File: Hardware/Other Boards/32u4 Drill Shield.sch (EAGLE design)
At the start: 16 parts, among them U2 XBEE-1B3

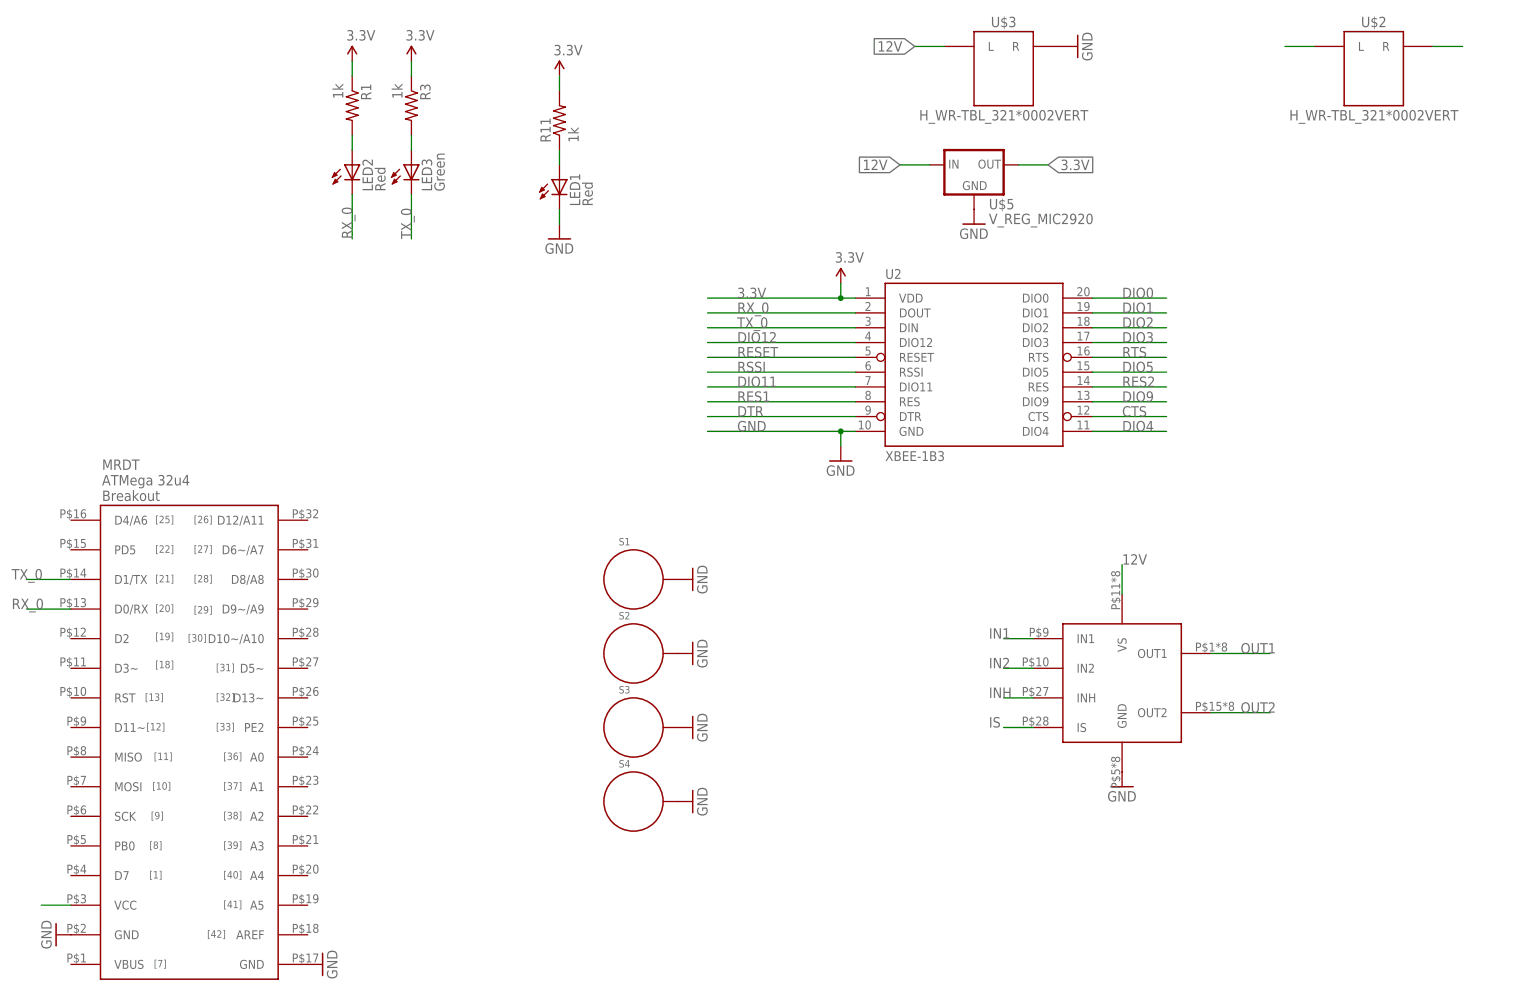
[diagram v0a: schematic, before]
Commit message: Finished shields for aux
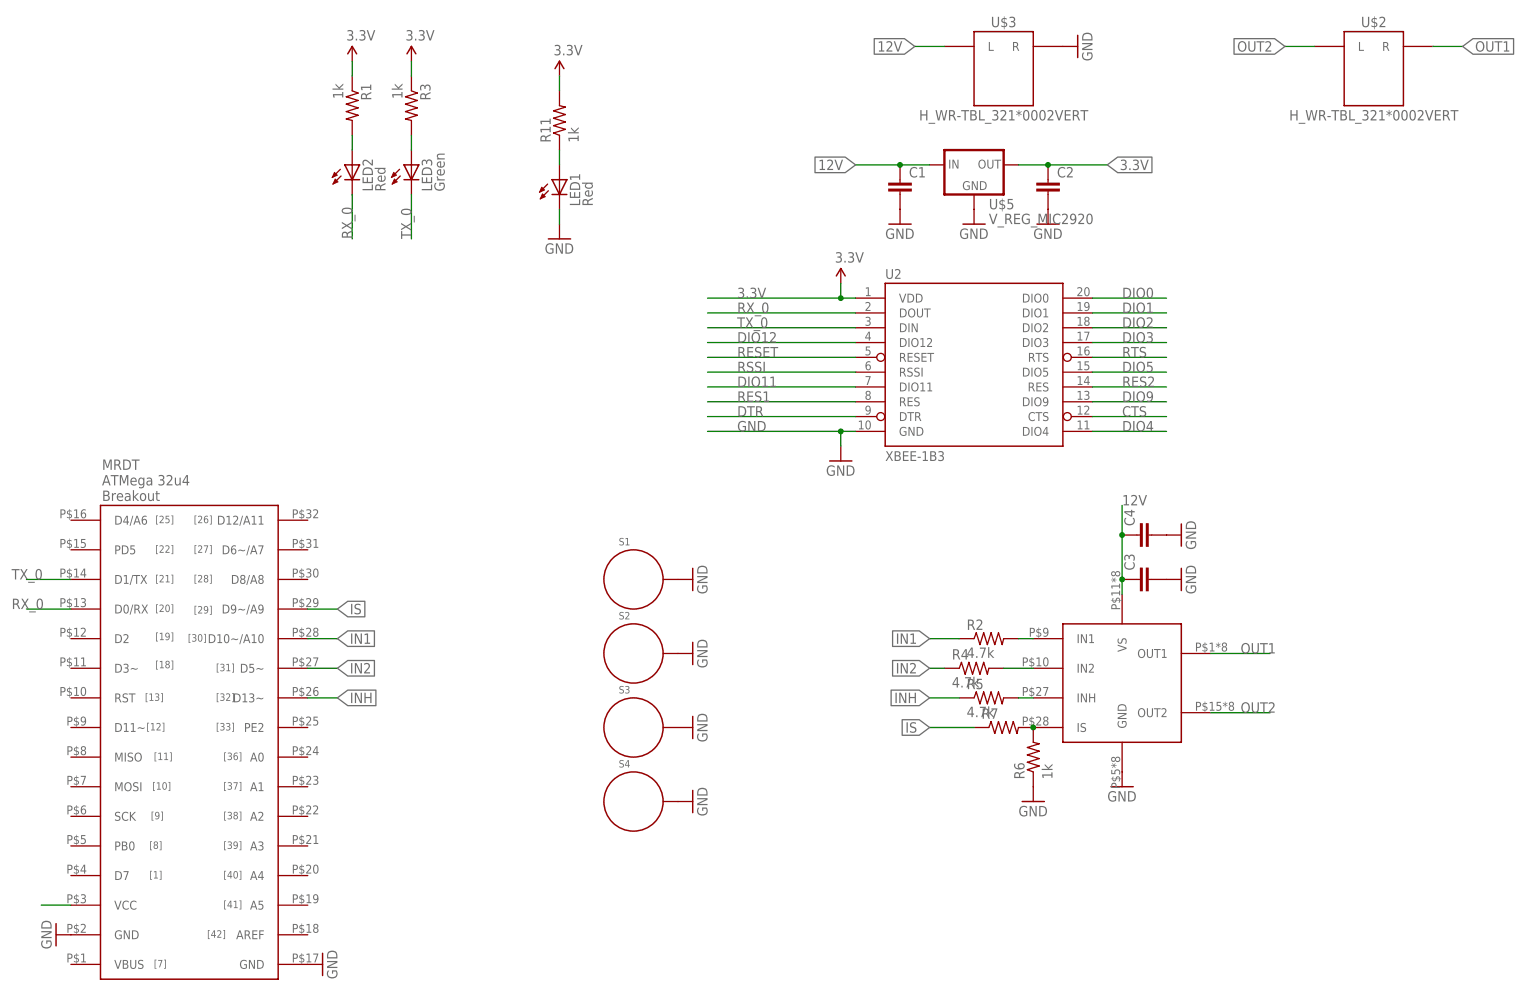
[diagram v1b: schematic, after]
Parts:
- added C1, C2, C3, C4: (no value), SparkFun-Passives:CAP1206
- added R2, R4, R5: 4.7k, SparkFun-Passives:RESISTOR1206
- added R6: 1k, SparkFun-Passives:RESISTOR1206
- added R7: (no value), SparkFun-Passives:RESISTOR1206
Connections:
- new net N$2: R2.2, U$4.IN1
- new net N$3: R4.2, U$4.IN2
- new net N$5: R5.2, U$4.INH
- new net N$6: R6.2, R7.2, U$4.IS
- net 12V: now also C1.1, C3.1, C4.1
- net 3.3V: now also C2.1
- net GND: now also C1.2, C2.2, C3.2, C4.2, R6.1
- net IN1: now also R2.1, U$1.D10~/A10; no longer U$4.IN1
- net IN2: now also R4.1, U$1.D5~; no longer U$4.IN2
- net INH: now also R5.1, U$1.D13~; no longer U$4.INH
- net IS: now also R7.1, U$1.D9~/A9; no longer U$4.IS
- net OUT1: now also U$2.R
- net OUT2: no longer U$2.R
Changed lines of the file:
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@@
 <part name="U$4" library="MRDT-2015-General" deviceset="BTM7752G" device=""/>
 <part name="GND10" library="SparkFun" deviceset="GND" device=""/>
+<part name="C1" library="SparkFun-Passives" deviceset="CAP" device="1206"/>
+<part name="C2" library="SparkFun-Passives" deviceset="CAP" device="1206"/>
+<part name="GND11" library="SparkFun" deviceset="GND" device=""/>
+<part name="GND12" library="SparkFun" deviceset="GND" device=""/>
+<part name="R2" library="SparkFun-Passives" deviceset="RESISTOR" device="1206" value="4.7k"/>
+<part name="R4" library="SparkFun-Passives" deviceset="RESISTOR" device="1206" value="4.7k"/>
+<part name="R5" library="SparkFun-Passives" deviceset="RESISTOR" device="1206" value="4.7k"/>
+<part name="R6" library="SparkFun-Passives" deviceset="RESISTOR" device="1206" value="1k"/>
+<part name="GND13" library="SparkFun" deviceset="GND" device=""/>
+<part name="R7" library="SparkFun-Passives" deviceset="RESISTOR" device="1206"/>
+<part name="C3" library="SparkFun-Passives" deviceset="CAP" device="1206"/>
+<part name="C4" library="SparkFun-Passives" deviceset="CAP" device="1206"/>
+<part name="GND14" library="SparkFun" deviceset="GND" device=""/>
+<part name="GND15" library="SparkFun" deviceset="GND" device=""/>
 </parts>
 <sheets>
@@
 <instance part="U$4" gate="G$1" x="185.42" y="53.34"/>
 <instance part="GND10" gate="1" x="185.42" y="35.56"/>
+<instance part="C1" gate="G$1" x="147.32" y="137.16"/>
+<instance part="C2" gate="G$1" x="172.72" y="137.16"/>
+<instance part="GND11" gate="1" x="147.32" y="132.08"/>
+<instance part="GND12" gate="1" x="172.72" y="132.08"/>
+<instance part="R2" gate="G$1" x="162.56" y="60.96"/>
+<instance part="R4" gate="G$1" x="160.02" y="55.88"/>
+<instance part="R5" gate="G$1" x="162.56" y="50.8"/>
+<instance part="R6" gate="G$1" x="170.18" y="40.64" rot="R90"/>
+<instance part="GND13" gate="1" x="170.18" y="33.02"/>
+<instance part="R7" gate="G$1" x="165.1" y="45.72"/>
+<instance part="C3" gate="G$1" x="190.5" y="71.12" rot="R90"/>
+<instance part="C4" gate="G$1" x="190.5" y="78.74" rot="R90"/>
+<instance part="GND14" gate="1" x="195.58" y="78.74" rot="R90"/>
+<instance part="GND15" gate="1" x="195.58" y="71.12" rot="R90"/>
 </instances>
 <busses>
@@
 <pinref part="GND10" gate="1" pin="GND"/>
 </segment>
+<segment>
+<pinref part="C1" gate="G$1" pin="2"/>
+<pinref part="GND11" gate="1" pin="GND"/>
+</segment>
+<segment>
+<pinref part="C2" gate="G$1" pin="2"/>
+<pinref part="GND12" gate="1" pin="GND"/>
+</segment>
+<segment>
+<pinref part="R6" gate="G$1" pin="1"/>
+<pinref part="GND13" gate="1" pin="GND"/>
+</segment>
+<segment>
+<pinref part="C4" gate="G$1" pin="2"/>
+<pinref part="GND14" gate="1" pin="GND"/>
+</segment>
+<segment>
+<pinref part="C3" gate="G$1" pin="2"/>
+<pinref part="GND15" gate="1" pin="GND"/>
+</segment>
 </net>
 <net name="RESET" class="0">
@@
 <pinref part="U$5" gate="G$1" pin="OUT"/>
 <wire x1="167.64" y1="142.24" x2="172.72" y2="142.24" width="0.1524" layer="91"/>
-<label x="172.72" y="142.24" size="1.778" layer="95" xref="yes"/>
+<label x="182.88" y="142.24" size="1.778" layer="95" xref="yes"/>
+<pinref part="C2" gate="G$1" pin="1"/>
+<wire x1="172.72" y1="142.24" x2="182.88" y2="142.24" width="0.1524" layer="91"/>
+<junction x="172.72" y="142.24"/>
 </segment>
 </net>
@@
 <pinref part="U$5" gate="G$1" pin="IN"/>
 <wire x1="152.4" y1="142.24" x2="147.32" y2="142.24" width="0.1524" layer="91"/>
-<label x="147.32" y="142.24" size="1.778" layer="95" rot="R180" xref="yes"/>
+<label x="139.7" y="142.24" size="1.778" layer="95" rot="R180" xref="yes"/>
+<pinref part="C1" gate="G$1" pin="1"/>
+<wire x1="147.32" y1="142.24" x2="139.7" y2="142.24" width="0.1524" layer="91"/>
+<junction x="147.32" y="142.24"/>
 </segment>
 <segment>
@@
 <segment>
 <pinref part="U$4" gate="G$1" pin="VS"/>
-<wire x1="185.42" y1="68.58" x2="185.42" y2="73.66" width="0.1524" layer="91"/>
-<label x="185.42" y="73.66" size="1.778" layer="95"/>
+<wire x1="185.42" y1="68.58" x2="185.42" y2="71.12" width="0.1524" layer="91"/>
+<label x="185.42" y="83.82" size="1.778" layer="95"/>
+<pinref part="C3" gate="G$1" pin="1"/>
+<wire x1="185.42" y1="71.12" x2="185.42" y2="78.74" width="0.1524" layer="91"/>
+<junction x="185.42" y="71.12"/>
+<pinref part="C4" gate="G$1" pin="1"/>
+<wire x1="185.42" y1="78.74" x2="185.42" y2="83.82" width="0.1524" layer="91"/>
+<junction x="185.42" y="78.74"/>
 </segment>
 </net>
@@
 <label x="205.74" y="58.42" size="1.778" layer="95"/>
 </segment>
+<segment>
+<pinref part="U$2" gate="G$1" pin="R"/>
+<wire x1="238.76" y1="162.56" x2="243.84" y2="162.56" width="0.1524" layer="91"/>
+<label x="243.84" y="162.56" size="1.778" layer="95" xref="yes"/>
+</segment>
 </net>
 <net name="OUT2" class="0">
@@
 </segment>
 <segment>
-<pinref part="U$2" gate="G$1" pin="R"/>
-<wire x1="238.76" y1="162.56" x2="243.84" y2="162.56" width="0.1524" layer="91"/>
-</segment>
-<segment>
 <pinref part="U$2" gate="G$1" pin="L"/>
 <wire x1="218.44" y1="162.56" x2="213.36" y2="162.56" width="0.1524" layer="91"/>
+<label x="213.36" y="162.56" size="1.778" layer="95" rot="R180" xref="yes"/>
+</segment>
+</net>
+<net name="N$2" class="0">
+<segment>
+<pinref part="U$4" gate="G$1" pin="IN1"/>
+<pinref part="R2" gate="G$1" pin="2"/>
+<wire x1="167.64" y1="60.96" x2="170.18" y2="60.96" width="0.1524" layer="91"/>
+</segment>
+</net>
+<net name="N$3" class="0">
+<segment>
+<pinref part="U$4" gate="G$1" pin="IN2"/>
+<pinref part="R4" gate="G$1" pin="2"/>
+<wire x1="165.1" y1="55.88" x2="170.18" y2="55.88" width="0.1524" layer="91"/>
+</segment>
+</net>
+<net name="N$5" class="0">
+<segment>
+<pinref part="U$4" gate="G$1" pin="INH"/>
+<pinref part="R5" gate="G$1" pin="2"/>
+<wire x1="167.64" y1="50.8" x2="170.18" y2="50.8" width="0.1524" layer="91"/>
 </segment>
 </net>
 <net name="IN1" class="0">
 <segment>
-<pinref part="U$4" gate="G$1" pin="IN1"/>
-<wire x1="170.18" y1="60.96" x2="165.1" y2="60.96" width="0.1524" layer="91"/>
-<label x="162.56" y="60.96" size="1.778" layer="95"/>
+<pinref part="R2" gate="G$1" pin="1"/>
+<wire x1="157.48" y1="60.96" x2="152.4" y2="60.96" width="0.1524" layer="91"/>
+<label x="152.4" y="60.96" size="1.778" layer="95" rot="R180" xref="yes"/>
+</segment>
+<segment>
+<pinref part="U$1" gate="G$1" pin="D10~/A10"/>
+<wire x1="45.72" y1="60.96" x2="50.8" y2="60.96" width="0.1524" layer="91"/>
+<label x="50.8" y="60.96" size="1.778" layer="95" xref="yes"/>
 </segment>
 </net>
 <net name="IN2" class="0">
 <segment>
-<pinref part="U$4" gate="G$1" pin="IN2"/>
-<wire x1="170.18" y1="55.88" x2="165.1" y2="55.88" width="0.1524" layer="91"/>
-<label x="162.56" y="55.88" size="1.778" layer="95"/>
+<pinref part="R4" gate="G$1" pin="1"/>
+<wire x1="154.94" y1="55.88" x2="152.4" y2="55.88" width="0.1524" layer="91"/>
+<label x="152.4" y="55.88" size="1.778" layer="95" rot="R180" xref="yes"/>
+</segment>
+<segment>
+<pinref part="U$1" gate="G$1" pin="D5~"/>
+<wire x1="45.72" y1="55.88" x2="50.8" y2="55.88" width="0.1524" layer="91"/>
+<label x="50.8" y="55.88" size="1.778" layer="95" xref="yes"/>
 </segment>
 </net>
 <net name="INH" class="0">
 <segment>
-<pinref part="U$4" gate="G$1" pin="INH"/>
-<wire x1="170.18" y1="50.8" x2="165.1" y2="50.8" width="0.1524" layer="91"/>
-<label x="162.56" y="50.8" size="1.778" layer="95"/>
+<pinref part="R5" gate="G$1" pin="1"/>
+<wire x1="157.48" y1="50.8" x2="152.4" y2="50.8" width="0.1524" layer="91"/>
+<label x="152.4" y="50.8" size="1.778" layer="95" rot="R180" xref="yes"/>
+</segment>
+<segment>
+<pinref part="U$1" gate="G$1" pin="D13~"/>
+<wire x1="45.72" y1="50.8" x2="50.8" y2="50.8" width="0.1524" layer="91"/>
+<label x="50.8" y="50.8" size="1.778" layer="95" xref="yes"/>
+</segment>
+</net>
+<net name="N$6" class="0">
+<segment>
+<pinref part="U$4" gate="G$1" pin="IS"/>
+<pinref part="R6" gate="G$1" pin="2"/>
+<pinref part="R7" gate="G$1" pin="2"/>
+<junction x="170.18" y="45.72"/>
+<pinref part="R7" gate="G$1" pin="2"/>
 </segment>
 </net>
 <net name="IS" class="0">
 <segment>
-<pinref part="U$4" gate="G$1" pin="IS"/>
-<wire x1="170.18" y1="45.72" x2="165.1" y2="45.72" width="0.1524" layer="91"/>
-<label x="162.56" y="45.72" size="1.778" layer="95"/>
-</segment>
-</net>
+<pinref part="U$1" gate="G$1" pin="D9~/A9"/>
+<wire x1="45.72" y1="66.04" x2="50.8" y2="66.04" width="0.1524" layer="91"/>
+<label x="50.8" y="66.04" size="1.778" layer="95" xref="yes"/>
+</segment>
+<segment>
+<pinref part="R7" gate="G$1" pin="1"/>
+<wire x1="160.02" y1="45.72" x2="152.4" y2="45.72" width="0.1524" layer="91"/>
+<label x="152.4" y="45.72" size="1.778" layer="95" rot="R180" xref="yes"/>
+</segment>
+</net>
